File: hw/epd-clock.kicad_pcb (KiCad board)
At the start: 4 copper layers, 86 x 43.7 mm, 60 parts, among them J1 Conn_01x24_MountingPin, Q1 Q_PMOS_GSD, Q2 Q_PMOS_GSD, Q3 IRLML6344, SW1 SW_Push, SW2 SW_Push, SW3 SW_Push, U1 ME2188AXXPG, U2 LM75C, U3 MSP430G2553IPW28, U4 AT25xxx, U5 PCF8563T, Y1 Crystal_Small

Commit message: epd-clock: hw v0.2
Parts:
- removed the R2 at (121.3, 118.5)
- removed the R3 at (117.9, 115.2)
- removed the R4 at (155.8, 115.1)
- added JP1: Jumper, Jumper:SolderJumper-2_P1.3mm_Open_RoundedPad1.0x1.5mm, B.Cu at (117.4, 122.6)
- added JP2: Jumper, Jumper:SolderJumper-2_P1.3mm_Open_RoundedPad1.0x1.5mm, B.Cu at (113.8, 113.6)
- added JP3: Jumper_3_Open, Jumper:SolderJumper-3_P1.3mm_Bridged12_RoundedPad1.0x1.5mm, B.Cu at (170.4, 102.5)
- added R6: 4.7K, Resistor_SMD:R_0603_1608Metric, B.Cu at (138.1, 104.7)
- added R7: 4.7K, Resistor_SMD:R_0603_1608Metric, B.Cu at (138.1, 106.2)
- C2: footprint Capacitor_SMD:C_0805_2012Metric -> Capacitor_SMD:C_1206_3216Metric
- Q3: footprint Package_TO_SOT_SMD:SOT-23 -> Package_TO_SOT_SMD:SOT-323_SC-70
- R1: value 0 -> 10K
- moved R1 5.66 mm to (121.3, 118.6)
- moved TP1 2.50 mm to (115.3, 99.1)
- moved TP2 2.50 mm to (117.8, 99.1)
- moved TP3 2.50 mm to (127.8, 99.1)
- moved TP4 2.50 mm to (125.3, 99.1)
- moved TP5 2.50 mm to (122.8, 99.1)
- moved TP6 2.50 mm to (120.3, 99.1)
- moved C16 1.17 mm to (154.9, 102.4)
- moved U2 1.11 mm to (160.4, 104.2)
- moved C8 1.09 mm to (155.0, 115.9), turned to 0 degrees
- moved Q1 0.81 mm to (120.7, 122.6), turned to 90 degrees
- moved C2 0.76 mm to (117.6, 117.8), turned to 90 degrees
- moved Y1 0.60 mm to (141.6, 119.5)
- moved C20 0.60 mm to (142.3, 117.9)
- moved C21 0.60 mm to (142.3, 123.0)
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- renumbered R11 to R10, R12 to R11, R13 to R12, R5 to R2, R6 to R3, R7 to R4, R8 to R5, R9 to R8, R10 to R9
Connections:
- R1 pad 1: Net-(C1-Pad1) -> /mcu/AIN
- R1 pad 2: Net-(BT1-Pad1) -> Net-(Q1-Pad3)
- Y1 pad 3: GND -> (no net)
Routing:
- net /mcu/SDA: track 13.6 -> 29.3 mm
- net /mcu/SCL: track 13.1 -> 22.7 mm
- net VCC: track 33.2 -> 27.7 mm, vias 1 -> 4
- net Net-(BT1-Pad1): track 50.8 -> 55.9 mm
- net Net-(C2-Pad1): track 7.60 -> 11.1 mm
- net Net-(C1-Pad1): track 8.58 -> 11.5 mm
- net /epd/BS1: track 15.7 -> 18.5 mm, vias 2 -> 0
- net /mcu/RST: track 20.4 -> 22.9 mm
- net /mcu/TEST: track 14.9 -> 17.4 mm
- net /mcu/UCA0RXD: track 15.8 -> 18.3 mm
- net /power/ADEN#: track 15.5 -> 13.6 mm
- net /epd/TSCL: track 32.3 -> 33.9 mm
- net Net-(C8-Pad1): track 13.1 -> 14.7 mm, vias 2 -> 0
- net /epd/VSL: track 11.0 -> 12.4 mm
- net /button/BT2: track 30.3 -> 31.5 mm
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- added copper zone on F.Cu, net GND
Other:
- outline, holes or cut-outs redrawn
- board text added: "3 wire"
- board text added: "4 wire"
- board text removed: "DC-DC-TP"

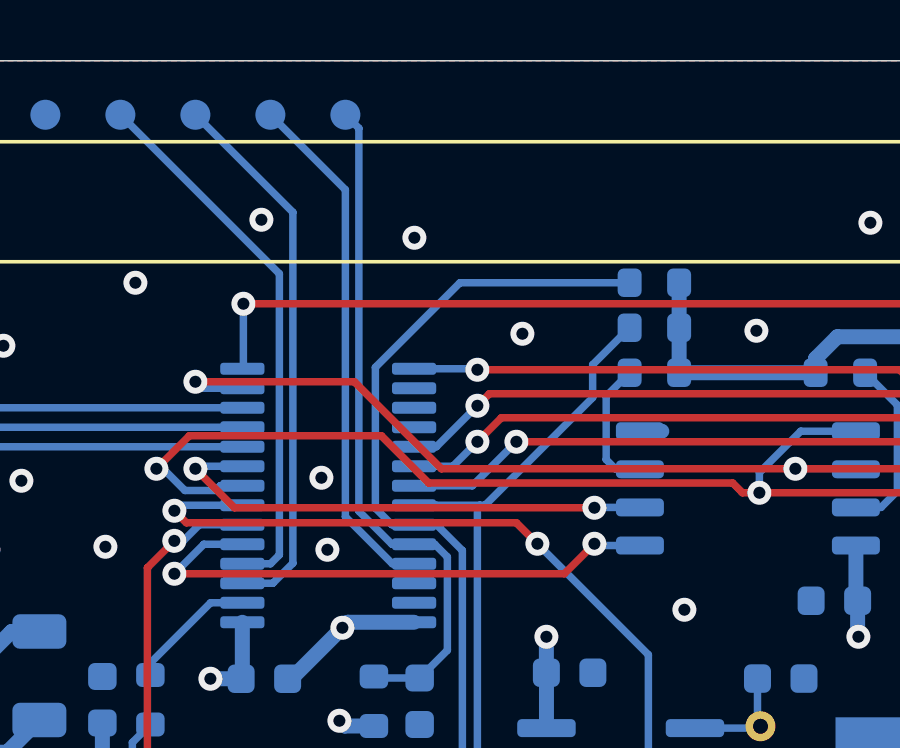
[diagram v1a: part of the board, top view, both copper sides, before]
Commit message: epd-clock hw: add i2c test point
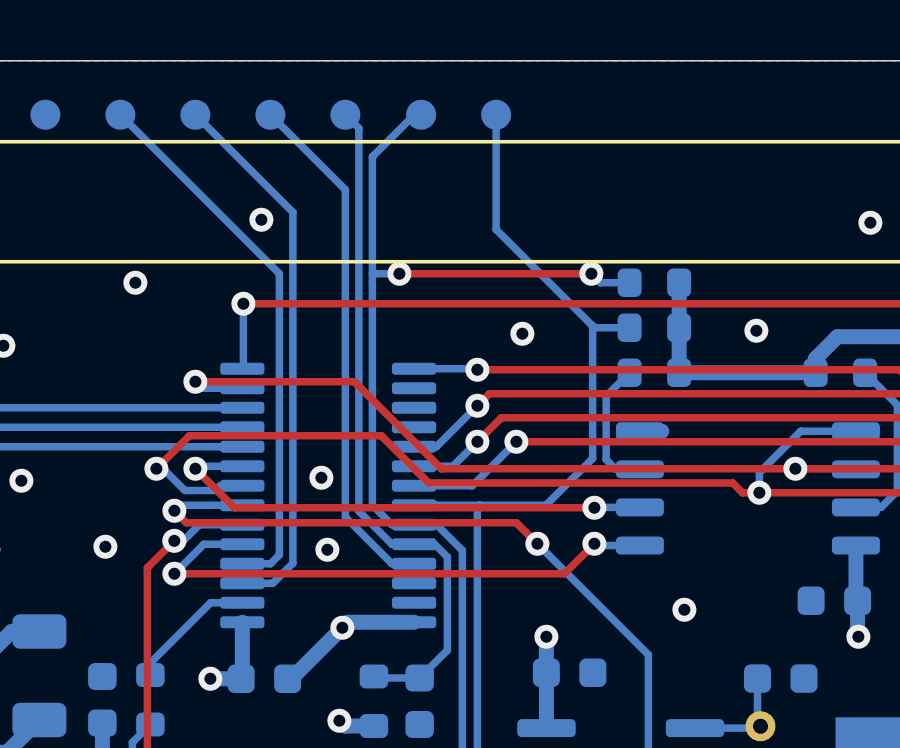
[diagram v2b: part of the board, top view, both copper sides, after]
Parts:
- added TP7: TestPoint, TestPoint:TestPoint_Pad_D1.0mm, B.Cu at (132.8, 99.1)
- added TP8: TestPoint, TestPoint:TestPoint_Pad_D1.0mm, B.Cu at (130.3, 99.1)
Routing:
- net /mcu/SCL: track 22.7 -> 33.1 mm
- net /mcu/SDA: track 29.3 -> 37.6 mm, vias 0 -> 2
- net GND: vias 69 -> 68
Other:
- board text added: "SCL"
- board text added: "SDA"

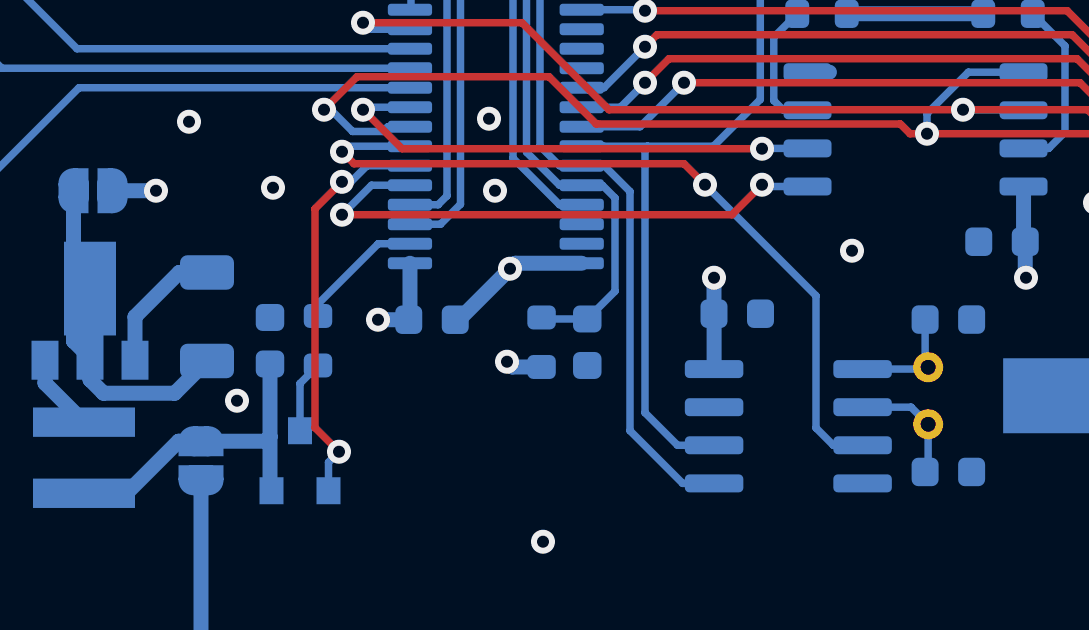
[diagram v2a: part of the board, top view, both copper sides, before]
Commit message: epd-clock: hw add wakeup pin pull up register
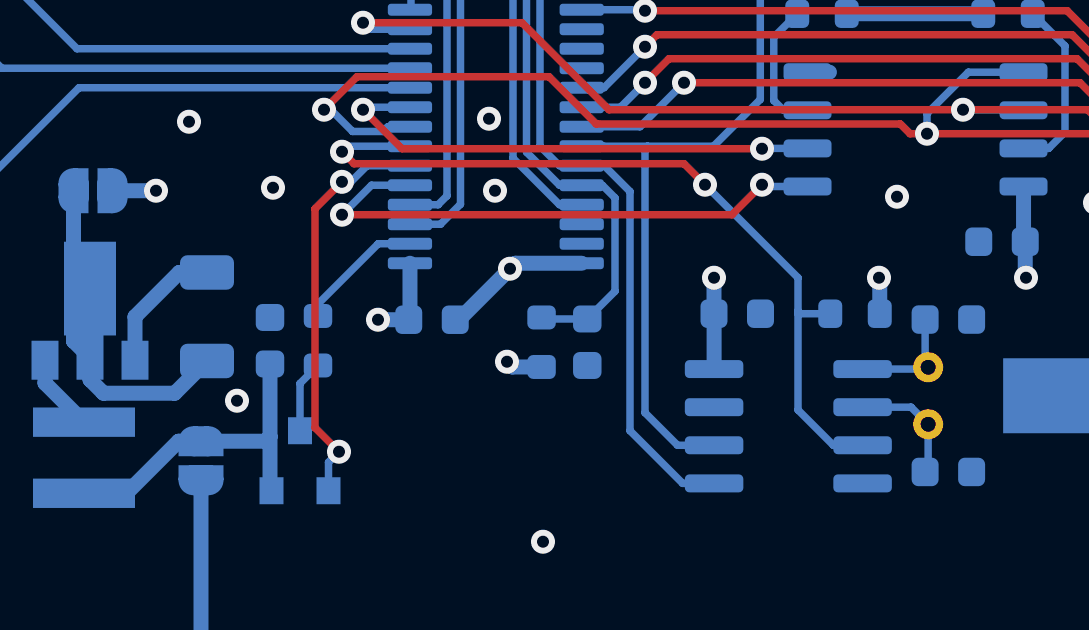
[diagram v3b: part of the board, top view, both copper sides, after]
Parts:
- added R13: 10K, Resistor_SMD:R_0603_1608Metric, B.Cu at (139.2, 117.7)
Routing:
- net +3V3: track 31.1 -> 32.4 mm, vias 11 -> 12
- net /rtc/INT: track 26.3 -> 27.4 mm

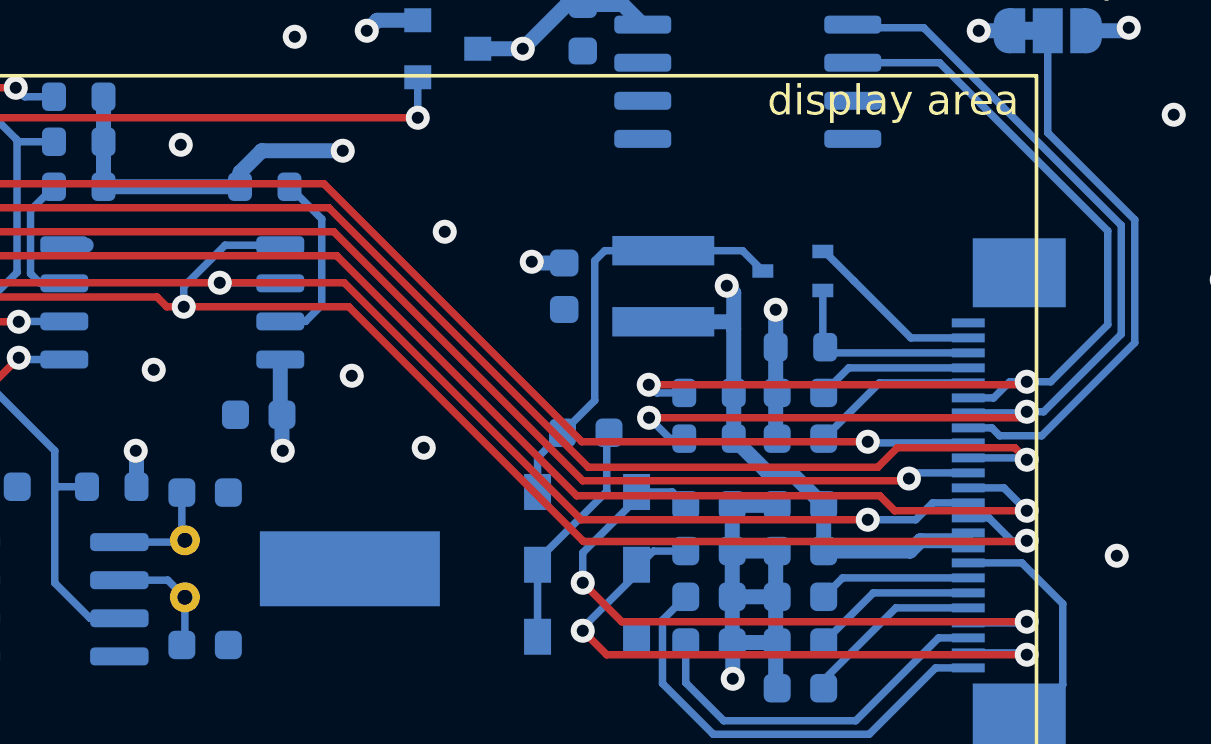
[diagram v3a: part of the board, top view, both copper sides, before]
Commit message: epd-clock: hw change C8 footprint
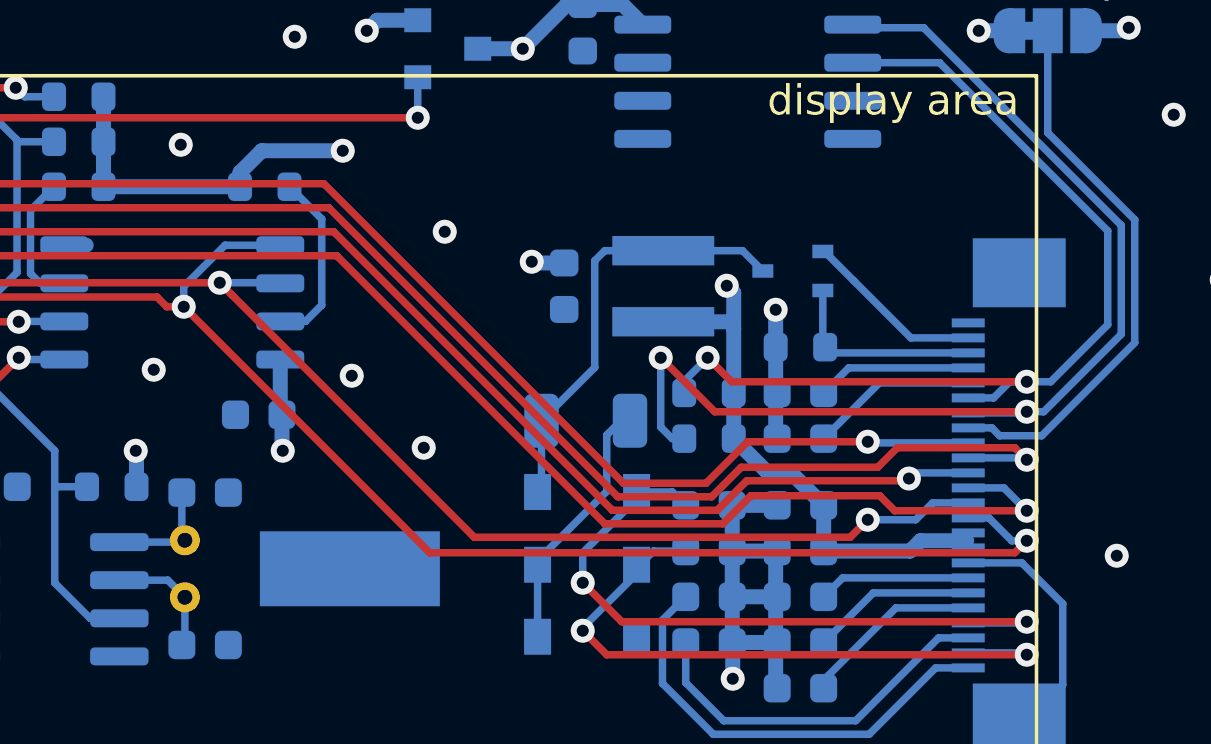
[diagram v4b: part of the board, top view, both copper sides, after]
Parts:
- C8: footprint Capacitor_SMD:C_0603_1608Metric -> Capacitor_SMD:C_1206_3216Metric
- moved C8 0.40 mm to (155.0, 115.5)
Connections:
- Y1 pad 3: (no net) -> GND
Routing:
- net /epd/TSDA: track 35.1 -> 37.1 mm
- net /epd/TSCL: track 33.9 -> 32.4 mm
- net /epd/BUSY: track 41.2 -> 42.4 mm
- net Net-(C8-Pad2): track 7.85 -> 8.71 mm
- net /mcu/EPD_RST#: track 46.7 -> 47.5 mm
- net /epd/DC#: track 41.9 -> 42.7 mm
- net /epd/CS#: track 46.1 -> 46.8 mm

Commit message: epd-clock: hw: v0.2
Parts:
- removed the C16 at (154.9, 102.4)
- removed the C5 at (159.1, 119.8)
- removed the C6 at (162.1, 118.3)
- removed the C7 at (159.1, 118.3)
- removed JP3: Jumper_3_Open, Jumper:SolderJumper-3_P1.3mm_Bridged12_RoundedPad1.0x1.5mm
- removed the U2 at (160.4, 104.2)
- added C10: 0.1uF/50V, Capacitor_SMD:C_0603_1608Metric, B.Cu at (155.7, 119.6)
- added C4: 1uF/25V, Capacitor_SMD:C_0603_1608Metric, B.Cu at (163.1, 119.6)
- added C9: 1uF/50V, Capacitor_SMD:C_0603_1608Metric, B.Cu at (160.0, 114.2)
- added R11: 4.7K, Resistor_SMD:R_0603_1608Metric, B.Cu at (129.6, 103.6)
- added R5: 4.7K, Resistor_SMD:R_0603_1608Metric, B.Cu at (169.6, 106.8)
- added R7: 10K, Resistor_SMD:R_0603_1608Metric, B.Cu at (144.3, 106.1)
- added R8: 10K, Resistor_SMD:R_0603_1608Metric, B.Cu at (144.3, 107.7)
- added R9: 10K, Resistor_SMD:R_0603_1608Metric, B.Cu at (138.1, 106.1)
- C12: value 1uF/25V -> 1uF/50V
- C3: value 1uF/25V -> 0.1uF/25V
- C8: value 4.7uF/50V -> 1uF/25V; footprint Capacitor_SMD:C_1206_3216Metric -> Capacitor_SMD:C_0603_1608Metric
- R2, R3: value 4.7K -> 10K
- moved R6 31.5 mm to (169.6, 105.2), turned to 0 degrees
- moved TP8 30.9 mm to (148.1, 124.4)
- moved TP7 28.3 mm to (145.5, 124.4)
- moved Q3 13.4 mm to (160.0, 123.8), turned to 90 degrees
- moved C12 12.5 mm to (160.0, 110.6), turned to 0 degrees
- moved L2 12.3 mm to (155.8, 123.2), turned to 90 degrees
- moved C15 11.5 mm to (163.1, 110.6), turned to 180 degrees
- moved C14 11.2 mm to (163.1, 112.4), turned to 180 degrees
- moved R3 11.0 mm to (163.1, 124.8), turned to 0 degrees
- moved C6 10.3 mm to (160.0, 119.6), turned to 180 degrees
- moved C13 10.3 mm to (163.1, 114.2)
- moved R4 10.00 mm to (163.1, 123.0)
- moved R2 8.80 mm to (153.9, 109.0), turned to 270 degrees
- moved R12 8.56 mm to (129.6, 105.2)
- moved Q2 8.41 mm to (156.4, 109.0)
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- renumbered C17 to C16, C18 to C17, C19 to C18, C20 to C19, C21 to C20, C22 to C21, C4 to C5, C9 to C6, C10 to C7, R5 to R10, R7 to R12, R8 to R13, R9 to R14, R10 to R15, R11 to R16, R12 to R17, R13 to R18, U3 to U2, U4 to U3, U5 to U4
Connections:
- C11 pad 1: /epd/VDD -> /epd/VPP
- C12 pad 1: /epd/VPP -> /epd/PREVGL
- C3 pad 1: /epd/VGH -> VCC
- C6 pad 1: VCC -> GND
- C6 pad 2: GND -> VCC
- C8 pad 1: Net-(C8-Pad1) -> /epd/VDD
- C8 pad 2: Net-(C8-Pad2) -> GND
- D1 pad 2: Net-(C8-Pad2) -> Net-(C10-Pad2)
- D2 pad 1: Net-(C8-Pad2) -> Net-(C10-Pad2)
- D3 pad 2: Net-(C8-Pad1) -> Net-(C10-Pad1)
- J1 pad 1: /epd/NC -> /epd/VCOM
- J1 pad 10: /mcu/EPD_RST# -> VCC
- J1 pad 11: /epd/DC# -> /epd/DIN
- J1 pad 12: /epd/CS# -> /epd/CLK
- J1 pad 13: /epd/CLK -> /epd/CS#
- J1 pad 14: /epd/DIN -> /epd/DC#
- J1 pad 15: VCC -> /mcu/EPD_RST#
- J1 pad 16: VCC -> /epd/BUSY
- J1 pad 18: /epd/VDD -> /epd/TSDA
- J1 pad 19: /epd/VPP -> /epd/TSCL
- J1 pad 2: /epd/GDR -> /epd/PREVGL
- J1 pad 20: /epd/VSH -> /epd/VGH
- J1 pad 21: /epd/PREVGH -> /epd/VGL
- J1 pad 22: /epd/VSL -> /epd/RESE
- J1 pad 23: /epd/PREVGL -> /epd/GDR
- J1 pad 24: /epd/VCOM -> /epd/NC
- J1 pad 3: /epd/RESE -> /epd/VSL
- J1 pad 4: /epd/VGL -> /epd/PREVGH
- J1 pad 5: /epd/VGH -> /epd/VSH
- J1 pad 6: /epd/TSCL -> /epd/VPP
- J1 pad 7: /epd/TSDA -> /epd/VDD
- J1 pad 8: /epd/BS1 -> GND
- J1 pad 9: /epd/BUSY -> VCC
- L2 pad 1: Net-(C8-Pad1) -> Net-(C10-Pad1)
- Q3 pad 3: Net-(C8-Pad1) -> Net-(C10-Pad1)
- R2 pad 1: VCC -> +3V3
- R2 pad 2: /epd/TSDA -> /mcu/EPD_PWR_EN
- R3 pad 1: VCC -> /epd/GDR
- R3 pad 2: /epd/TSCL -> GND
- R4 pad 1: GND -> /epd/RESE
- R4 pad 2: /epd/RESE -> GND
- R6 pad 1: +3V3 -> VCC
- R6 pad 2: /mcu/SDA -> /epd/TSCL
- U2 pad 15: /epd/BUSY -> /epd/DIN
- U2 pad 19: /mcu/EPD_RST# -> /epd/CS#
- U2 pad 21: /epd/CS# -> /mcu/EPD_RST#
- U2 pad 8: /epd/DIN -> /epd/BUSY
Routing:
- net /epd/TSDA: track 37.1 -> 17.5 mm, vias 2 -> 0
- net /epd/BS1: track 18.5 -> 0.00 mm
- net Net-(C10-Pad1): track 0.00 -> 16.6 mm
- net Net-(C8-Pad1): track 14.7 -> 0.00 mm
- net /epd/TSCL: track 32.4 -> 20.1 mm, vias 2 -> 0
- net /epd/PREVGH: track 23.6 -> 11.6 mm, vias 2 -> 0
- net /flash/MISO: track 17.0 -> 29.0 mm
- net /epd/CLK: track 54.5 -> 65.7 mm
- net GND: track 63.9 -> 53.0 mm, vias 68 -> 46
- net /epd/VCOM: track 15.1 -> 4.55 mm
- net /epd/DIN: track 63.6 -> 53.1 mm
- net /epd/PREVGL: track 22.4 -> 12.5 mm, vias 2 -> 0
- net /epd/BUSY: track 42.4 -> 52.1 mm
- net Net-(C10-Pad2): track 0.00 -> 8.97 mm
- net Net-(C8-Pad2): track 8.71 -> 0.00 mm
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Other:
- board text added: "1"
- board text added: "24"
- board text removed: "3 wire"
- board text removed: "4 wire"

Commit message: epd-clock: hw v0.2
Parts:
- removed TP7, TP8: TestPoint, TestPoint:TestPoint_Pad_D1.0mm
- C10: footprint Capacitor_SMD:C_0603_1608Metric -> Capacitor_SMD:C_0805_2012Metric
- Q3: footprint Package_TO_SOT_SMD:SOT-323_SC-70 -> Package_TO_SOT_SMD:SOT-23
- moved R4 6.79 mm to (156.5, 121.2), turned to 180 degrees
- moved R3 6.74 mm to (156.5, 123.2), turned to 180 degrees
- moved L2 5.95 mm to (158.6, 118.0), turned to 270 degrees
- moved C6 5.47 mm to (154.5, 119.2), turned to 0 degrees
- moved C12 4.78 mm to (155.3, 109.8), turned to 180 degrees
- moved C9 4.67 mm to (158.6, 109.8), turned to 180 degrees
- moved D1 4.33 mm to (154.5, 113.0), turned to 270 degrees
- moved C3 4.33 mm to (163.3, 118.6)
- moved C7 4.30 mm to (163.3, 120.2)
- moved D3 3.96 mm to (159.3, 113.0), turned to 270 degrees
- moved C10 3.09 mm to (154.5, 116.8), turned to 180 degrees
- moved C4 2.96 mm to (163.3, 122.5)
- moved C5 2.91 mm to (163.3, 124.1)
- moved Q2 2.85 mm to (156.4, 106.2)
- moved R2 2.85 mm to (153.9, 106.2)
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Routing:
- net /mcu/SDA: track 38.9 -> 24.5 mm
- net GND: track 53.0 -> 39.3 mm, vias 46 -> 54
- net /mcu/SCL: track 33.5 -> 21.1 mm
- net /epd/BUSY: track 52.1 -> 57.9 mm
- net /epd/GDR: track 7.75 -> 12.3 mm
- net /flash/CS: track 23.8 -> 19.8 mm
- net Net-(C10-Pad2): track 8.97 -> 5.45 mm
- net /epd/RESE: track 10.1 -> 13.6 mm
- net VCC: track 21.8 -> 18.4 mm
- net Net-(C10-Pad1): track 16.6 -> 13.3 mm
- net /mcu/EPD_PWR_EN: track 35.1 -> 38.3 mm
- net /epd/TSCL: track 20.1 -> 22.4 mm
- net /epd/PREVGL: track 12.5 -> 14.7 mm, vias 0 -> 2
- net /epd/CLK: track 65.7 -> 67.8 mm
- net /power/ADEN#: track 15.3 -> 13.3 mm
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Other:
- board text removed: "SCL"
- board text removed: "SDA"

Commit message: hw: 合并电源网络
取消墨水屏电源控制mos与独立电源域，墨水屏使用深度休眠模式，共用主
电源域。
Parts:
- removed the Q2 at (156.4, 106.2)
- removed the R2 at (153.9, 106.2)
- removed the R7 at (144.3, 106.1)
- removed the R8 at (144.3, 107.7)
- C10: value 0.1uF/50V -> 4.7uF/50V
- L2: value 47uH -> 10uH
- R2: renamed from R3; value 10K -> 1M
- R3: renamed from R4; value 4.7 -> 3R
- moved R11 3.15 mm to (144.4, 107.7)
- renumbered Q3 to Q2, R13 to R10, R14 to R11, R15 to R12, R16 to R13, R17 to R14, R18 to R15, R5 to R4, R6 to R5, R9 to R6, R10 to R7, R11 to R8, R12 to R9
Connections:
- C3 pad 1: VCC -> +3V3
- C6 pad 2: VCC -> +3V3
- C7 pad 1: VCC -> +3V3
- J1 pad 10: VCC -> +3V3
- J1 pad 9: VCC -> +3V3
- L2 pad 2: VCC -> +3V3
- R4 pad 1: VCC -> +3V3
- R5 pad 1: VCC -> +3V3
- Y1 pad 3: GND -> (no net)
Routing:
- net /mcu/EPD_PWR_EN: track 38.3 -> 0.00 mm, vias 2 -> 0
- net VCC: track 18.4 -> 0.00 mm, vias 5 -> 0
- net /epd/CLK: track 67.8 -> 61.3 mm
- net +3V3: track 38.2 -> 44.0 mm, vias 13 -> 17
- net Net-(R11-Pad1): track 9.34 -> 5.52 mm
- net /epd/DIN: track 52.9 -> 50.4 mm
- removed copper zone on In1.Cu.PWR, net VCC
